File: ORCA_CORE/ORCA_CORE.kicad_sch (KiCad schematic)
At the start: 12 parts, among them J18 +3V3_motor, J19 +5Vin_cpu, J23 md_arm, J24 md_fork, J25 servo_arm, J34 cpu_male_1, J35 hat_female_1, J36 cpu_male_1, J37 hat_female_1, J38 servo_arm, J39 md_arm, J40 md_fork

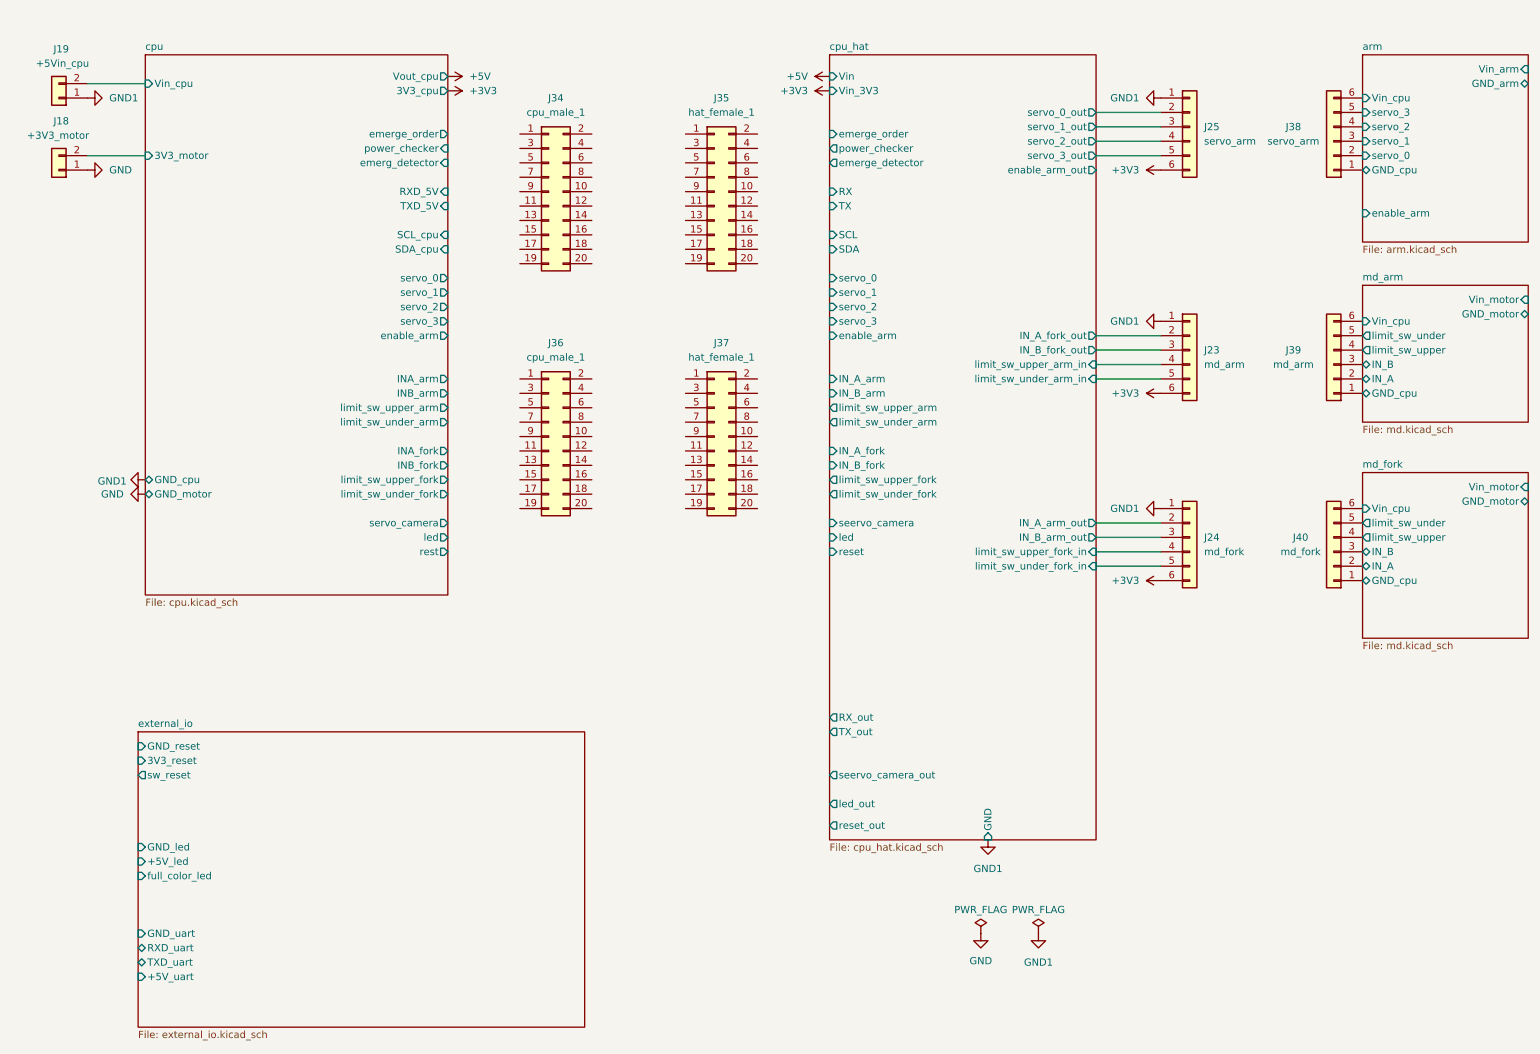
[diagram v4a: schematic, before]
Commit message: complete attaching footprint of CORE
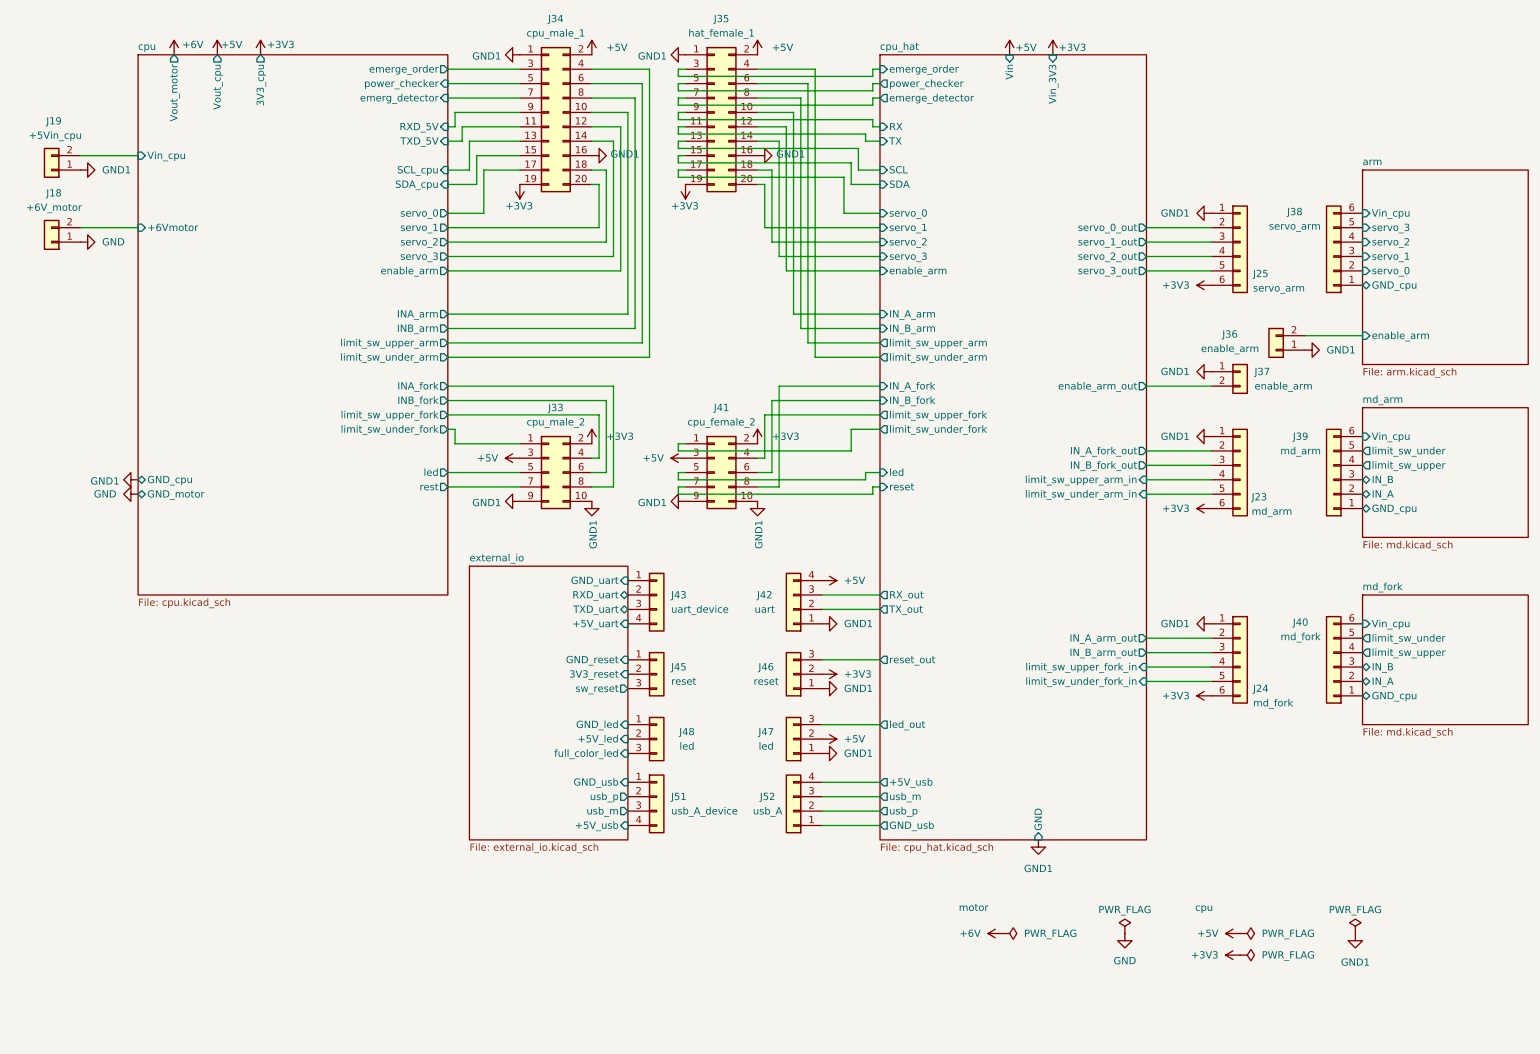
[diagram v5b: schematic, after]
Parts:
- removed J36: cpu_male_1, Connector_PinHeader_2.54mm:PinHeader_2x10_P2.54mm_Vertical, symbol Connector_Generic:Conn_02x10_Odd_Even
- removed J37: hat_female_1, Connector_PinHeader_2.54mm:PinHeader_2x10_P2.54mm_Vertical, symbol Connector_Generic:Conn_02x10_Odd_Even
- added J33: cpu_male_2, Connector_PinHeader_2.54mm:PinHeader_2x05_P2.54mm_Vertical, symbol Connector_Generic:Conn_02x05_Odd_Even
- added J36: enable_arm, Connector_JST:JST_XH_S2B-XH-A_1x02_P2.50mm_Horizontal, symbol Connector_Generic:Conn_01x02
- added J37: enable_arm, Connector_JST:JST_XH_B2B-XH-A_1x02_P2.50mm_Vertical, symbol Connector_Generic:Conn_01x02
- added J41: cpu_female_2, Connector_PinHeader_2.54mm:PinHeader_2x05_P2.54mm_Vertical, symbol Connector_Generic:Conn_02x05_Odd_Even
- added J42: uart, Connector_JST:JST_XH_B4B-XH-A_1x04_P2.50mm_Vertical, symbol Connector_Generic:Conn_01x04
- added J43: uart_device, Connector_JST:JST_XH_S4B-XH-A_1x04_P2.50mm_Horizontal, symbol Connector_Generic:Conn_01x04
- added J45: reset, Connector_JST:JST_XH_S3B-XH-A_1x03_P2.50mm_Horizontal, symbol Connector_Generic:Conn_01x03
- added J46: reset, Connector_JST:JST_XH_B3B-XH-A_1x03_P2.50mm_Vertical, symbol Connector_Generic:Conn_01x03
- added J47, J48: led, Connector_JST:JST_XH_B3B-XH-A_1x03_P2.50mm_Vertical, symbol Connector_Generic:Conn_01x03
- added J51: usb_A_device, Connector_JST:JST_XH_S4B-XH-A_1x04_P2.50mm_Horizontal, symbol Connector_Generic:Conn_01x04
- added J52: usb_A, Connector_JST:JST_XH_B4B-XH-A_1x04_P2.50mm_Vertical, symbol Connector_Generic:Conn_01x04
- J18: value +3V3_motor -> +6V_motor
- J23, J24, J25: footprint (none) -> Connector_JST:JST_XH_B6B-XH-A_1x06_P2.50mm_Vertical
- J38, J39, J40: footprint (none) -> Connector_JST:JST_XH_S6B-XH-A_1x06_P2.50mm_Horizontal
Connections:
- net +3V3: now also J34.19 (Pin_19), J35.19 (Pin_19), J33.2 (Pin_2), J41.2 (Pin_2), J46.2 (Pin_2)
- net +5V: now also J34.2 (Pin_2), J35.2 (Pin_2), J33.3 (Pin_3), J41.3 (Pin_3), J42.4 (Pin_4), J47.2 (Pin_2)
- net GND1: now also J34.1 (Pin_1), J34.16 (Pin_16), J35.1 (Pin_1), J35.16 (Pin_16), J33.10 (Pin_10), J33.9 (Pin_9), J36.1 (Pin_1), J37.1 (Pin_1), J41.10 (Pin_10), J41.9 (Pin_9), J42.1 (Pin_1), J46.1 (Pin_1), J47.1 (Pin_1)
- net arm/enable_arm: now also J36.2 (Pin_2)
- net cpu/INA_arm: now also J34.10 (Pin_10)
- net cpu/INA_fork: now also J33.8 (Pin_8)
- net cpu/INB_arm: now also J34.8 (Pin_8)
- net cpu/INB_fork: now also J33.6 (Pin_6)
- net cpu/RXD_5V: now also J34.9 (Pin_9)
- net cpu/SCL_cpu: now also J34.13 (Pin_13)
- net cpu/SDA_cpu: now also J34.15 (Pin_15)
- net cpu/TXD_5V: now also J34.11 (Pin_11)
- net cpu/emerg_detector: now also J34.7 (Pin_7)
- net cpu/emerge_order: now also J34.3 (Pin_3)
- net cpu/enable_arm: now also J34.12 (Pin_12)
- net cpu/led: now also J33.5 (Pin_5)
- net cpu/limit_sw_under_arm: now also J34.4 (Pin_4)
- net cpu/limit_sw_under_fork: now also J33.1 (Pin_1)
- net cpu/limit_sw_upper_arm: now also J34.6 (Pin_6)
- net cpu/limit_sw_upper_fork: now also J33.4 (Pin_4)
- net cpu/power_checker: now also J34.5 (Pin_5)
- net cpu/rest: now also J33.7 (Pin_7)
- net cpu/servo_0: now also J34.17 (Pin_17)
- net cpu/servo_1: now also J34.20 (Pin_20)
- net cpu/servo_2: now also J34.18 (Pin_18)
- net cpu/servo_3: now also J34.14 (Pin_14)
- net cpu_hat/IN_A_arm: now also J35.10 (Pin_10)
- net cpu_hat/IN_A_fork: now also J41.8 (Pin_8)
- net cpu_hat/IN_B_arm: now also J35.8 (Pin_8)
- net cpu_hat/IN_B_fork: now also J41.6 (Pin_6)
- net cpu_hat/RX: now also J35.9 (Pin_9)
- net cpu_hat/RX_out: now also J42.3 (Pin_3)
- net cpu_hat/SCL: now also J35.13 (Pin_13)
- net cpu_hat/SDA: now also J35.15 (Pin_15)
- net cpu_hat/TX: now also J35.11 (Pin_11)
- net cpu_hat/TX_out: now also J42.2 (Pin_2)
- net cpu_hat/emerge_detector: now also J35.7 (Pin_7)
- net cpu_hat/emerge_order: now also J35.3 (Pin_3)
- net cpu_hat/enable_arm: now also J35.12 (Pin_12)
- net cpu_hat/enable_arm_out: now also J37.2 (Pin_2)
- net cpu_hat/led: now also J41.5 (Pin_5)
- net cpu_hat/led_out: now also J47.3 (Pin_3)
- net cpu_hat/limit_sw_under_arm: now also J35.4 (Pin_4)
- net cpu_hat/limit_sw_under_fork: now also J41.1 (Pin_1)
- net cpu_hat/limit_sw_upper_arm: now also J35.6 (Pin_6)
- net cpu_hat/limit_sw_upper_fork: now also J41.4 (Pin_4)
- net cpu_hat/power_checker: now also J35.5 (Pin_5)
- net cpu_hat/reset: now also J41.7 (Pin_7)
- net cpu_hat/reset_out: now also J46.3 (Pin_3)
- net cpu_hat/servo_0: now also J35.17 (Pin_17)
- net cpu_hat/servo_1: now also J35.20 (Pin_20)
- net cpu_hat/servo_2: now also J35.18 (Pin_18)
- net cpu_hat/servo_3: now also J35.14 (Pin_14)
- net external_io/+5V_led: now also J48.2 (Pin_2)
- net external_io/+5V_uart: now also J43.4 (Pin_4)
- net external_io/3V3_reset: now also J45.2 (Pin_2)
- net external_io/GND_led: now also J48.1 (Pin_1)
- net external_io/GND_reset: now also J45.1 (Pin_1)
- net external_io/GND_uart: now also J43.1 (Pin_1)
- net external_io/RXD_uart: now also J43.2 (Pin_2)
- net external_io/TXD_uart: now also J43.3 (Pin_3)
- net external_io/full_color_led: now also J48.3 (Pin_3)
- net external_io/sw_reset: now also J45.3 (Pin_3)
- net cpu/3V3_motor renamed cpu/+6Vmotor
- new net cpu_hat/+5V_usb: J52.4 (Pin_4)
- new net cpu_hat/GND_usb: J52.1 (Pin_1)
- new net cpu_hat/usb_m: J52.3 (Pin_3)
- new net cpu_hat/usb_p: J52.2 (Pin_2)
- new net external_io/+5V_usb: J51.4 (Pin_4)
- new net external_io/GND_usb: J51.1 (Pin_1)
- new net external_io/usb_m: J51.3 (Pin_3)
- new net external_io/usb_p: J51.2 (Pin_2)
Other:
- sheet arm ports: added none; removed GND_arm, Vin_arm
- sheet cpu ports: added +6Vmotor, Vout_motor; removed 3V3_motor, servo_camera
- sheet cpu_hat ports: added +5V_usb, GND_usb, usb_m, usb_p; removed seervo_camera, seervo_camera_out
- sheet external_io ports: added +5V_usb, GND_usb, usb_m, usb_p; removed none
- sheet md_arm ports: added none; removed GND_motor, Vin_motor
- sheet md_fork ports: added none; removed GND_motor, Vin_motor
- note added: "cpu"
- note added: "motor"
- moved on the sheet: J18, J19, J23, J24, J25, J34, J35, J38, J39, J40

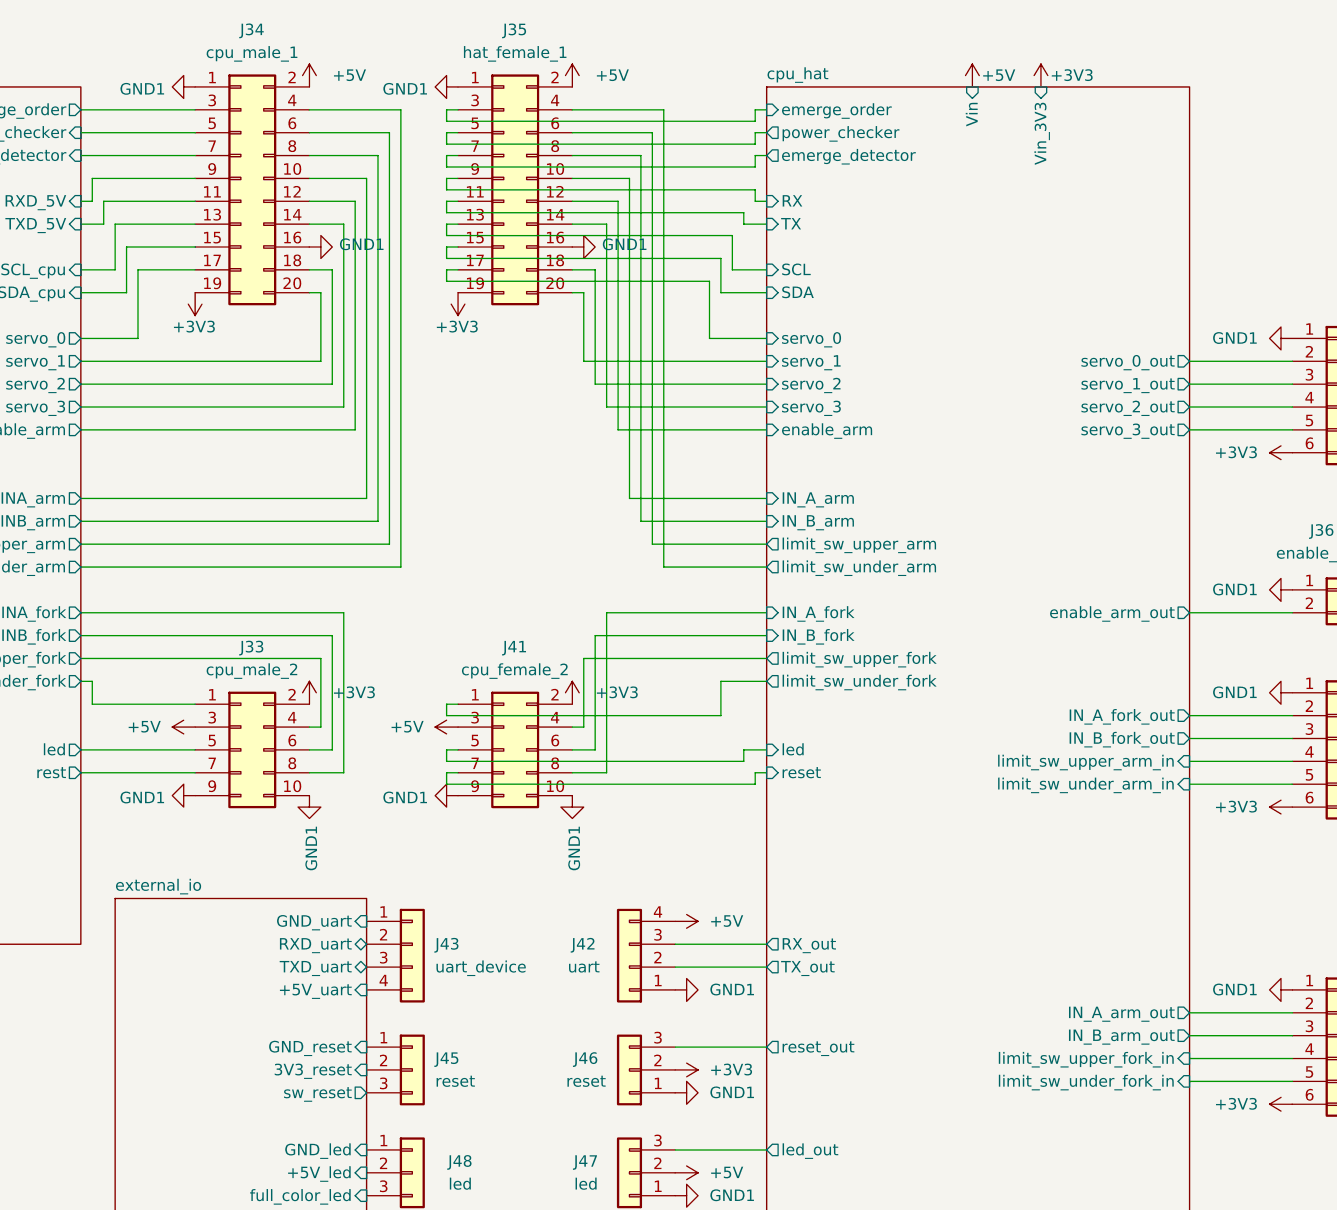
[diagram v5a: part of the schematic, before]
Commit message: place most of footprints. test replicate
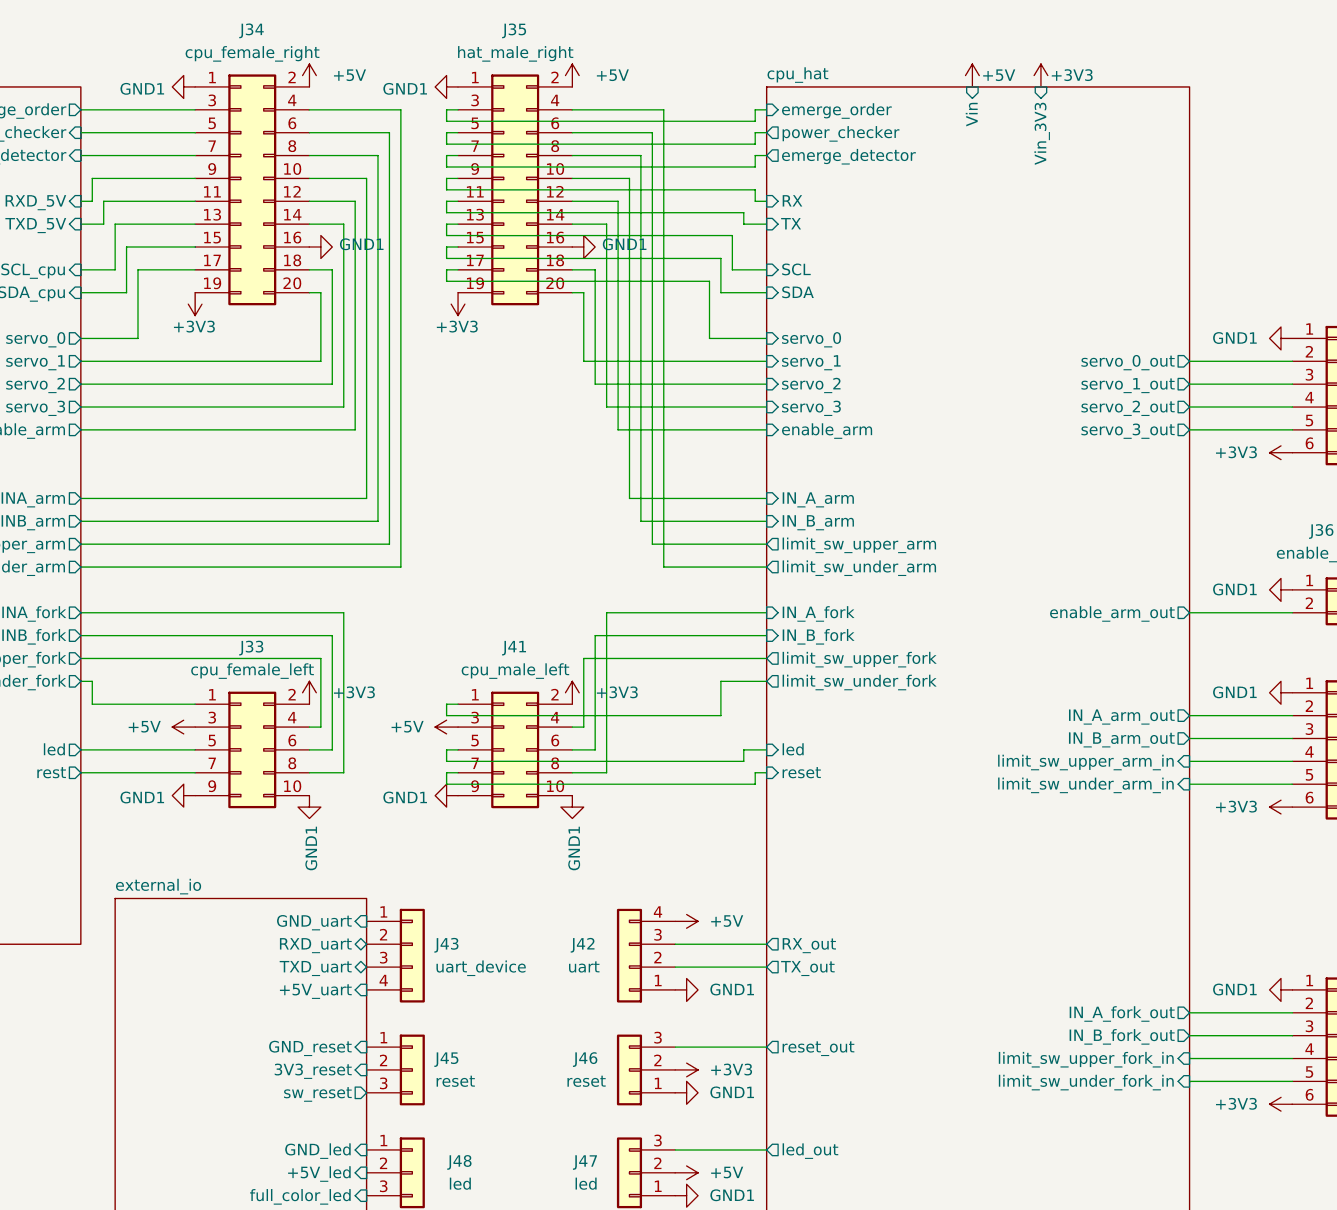
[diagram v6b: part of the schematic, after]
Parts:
- J33: value cpu_male_2 -> cpu_female_left; footprint Connector_PinHeader_2.54mm:PinHeader_2x05_P2.54mm_Vertical -> Connector_PinSocket_2.54mm:PinSocket_2x05_P2.54mm_Vertical
- J34: value cpu_male_1 -> cpu_female_right; footprint Connector_PinHeader_2.54mm:PinHeader_2x10_P2.54mm_Vertical -> Connector_PinSocket_2.54mm:PinSocket_2x10_P2.54mm_Vertical
- J35: value hat_female_1 -> hat_male_right
- J41: value cpu_female_2 -> cpu_male_left
- J45: footprint Connector_JST:JST_XH_S3B-XH-A_1x03_P2.50mm_Horizontal -> Connector_JST:JST_XH_B3B-XH-A_1x03_P2.50mm_Vertical
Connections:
- net cpu_hat/IN_A_arm_out: now also J23.2 (Pin_2); no longer J24.2 (Pin_2)
- net cpu_hat/IN_A_fork_out: now also J24.2 (Pin_2); no longer J23.2 (Pin_2)
- net cpu_hat/IN_B_arm_out: now also J23.3 (Pin_3); no longer J24.3 (Pin_3)
- net cpu_hat/IN_B_fork_out: now also J24.3 (Pin_3); no longer J23.3 (Pin_3)
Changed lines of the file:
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@@
 			)
 		)
-		(property "Footprint" "Connector_JST:JST_XH_S3B-XH-A_1x03_P2.50mm_Horizontal"
+		(property "Footprint" "Connector_JST:JST_XH_B3B-XH-A_1x03_P2.50mm_Vertical"
 			(at 127 128.27 0)
 			(effects
@@
 		(on_board yes)
 		(dnp no)
-		(fields_autoplaced yes)
 		(property "Reference" "J33"
 			(at 109.22 81.28 0)
@@
 			)
 		)
-		(property "Value" "cpu_male_2"
+		(property "Value" "cpu_female_left"
 			(at 109.22 83.82 0)
 			(effects
@@
 			)
 		)
-		(property "Footprint" "Connector_PinHeader_2.54mm:PinHeader_2x05_P2.54mm_Vertical"
+		(property "Footprint" "Connector_PinSocket_2.54mm:PinSocket_2x05_P2.54mm_Vertical"
 			(at 107.95 92.71 0)
 			(effects
@@
 			)
 		)
-		(property "Value" "cpu_female_2"
+		(property "Value" "cpu_male_left"
 			(at 138.43 83.82 0)
 			(effects
@@
 		(on_board yes)
 		(dnp no)
-		(fields_autoplaced yes)
 		(property "Reference" "J34"
 			(at 109.22 12.7 0)
@@
 			)
 		)
-		(property "Value" "cpu_male_1"
+		(property "Value" "cpu_female_right"
 			(at 109.22 15.24 0)
 			(effects
@@
 			)
 		)
-		(property "Footprint" "Connector_PinHeader_2.54mm:PinHeader_2x10_P2.54mm_Vertical"
+		(property "Footprint" "Connector_PinSocket_2.54mm:PinSocket_2x10_P2.54mm_Vertical"
 			(at 107.95 29.21 0)
 			(effects
@@
 			)
 		)
-		(property "Value" "hat_female_1"
+		(property "Value" "hat_male_right"
 			(at 138.43 15.24 0)
 			(effects
@@
 		)
 		(pin "IN_B_fork_out" output
-			(at 213.36 91.44 0)
+			(at 213.36 124.46 0)
 			(effects
 				(font
@@
 		)
 		(pin "IN_B_arm_out" output
-			(at 213.36 124.46 0)
+			(at 213.36 91.44 0)
 			(effects
 				(font
@@
 		)
 		(pin "IN_A_arm_out" output
-			(at 213.36 121.92 0)
+			(at 213.36 88.9 0)
 			(effects
 				(font
@@
 		)
 		(pin "IN_A_fork_out" output
-			(at 213.36 88.9 0)
+			(at 213.36 121.92 0)
 			(effects
 				(font
